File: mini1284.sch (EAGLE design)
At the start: 25 parts, among them U1 ATmega1284P-AU, Y1 16MHz

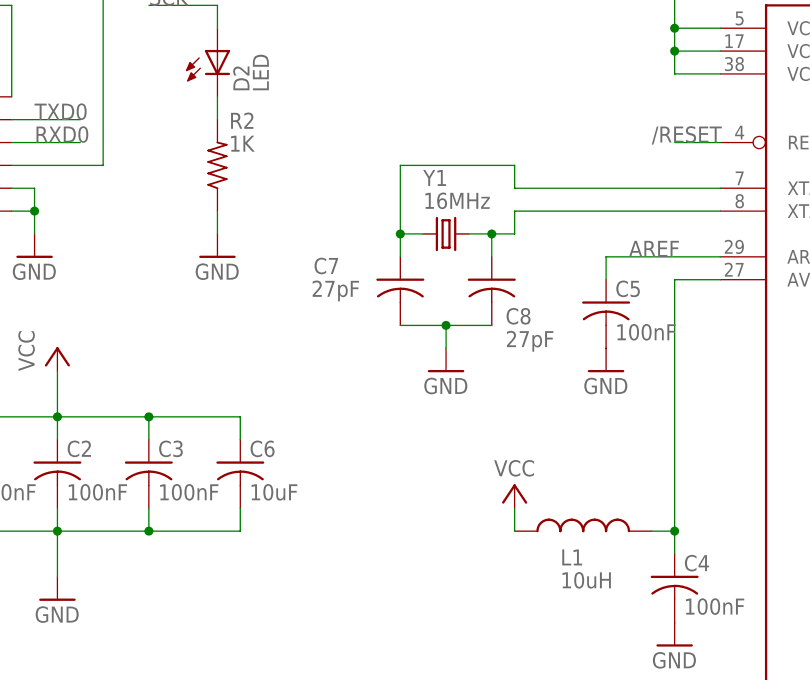
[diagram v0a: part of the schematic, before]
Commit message: Change to Epson crystal.
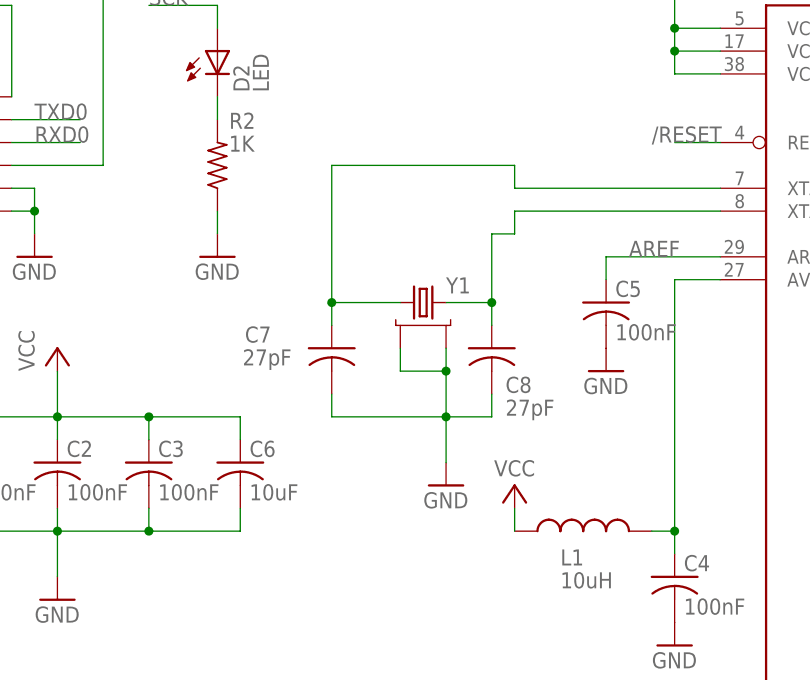
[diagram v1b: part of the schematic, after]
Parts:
- Y1: value 16MHz -> (none); device _jc:CRYSTALABM2 -> _jc:CRYSTAL-2GNDTSX3225
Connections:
- net GND: now also Y1.2, Y1.4
- net N$2: now also Y1.3; no longer Y1.2
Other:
- moved on the sheet: C7, C8
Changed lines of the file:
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@@
 <part name="JP4" library="SparkFun" deviceset="M09" device="" value="M09"/>
 <part name="GND5" library="SparkFun" deviceset="GND" device=""/>
-<part name="Y1" library="_jc" deviceset="CRYSTAL" device="ABM2" value="16MHz"/>
 <part name="P+7" library="supply1" deviceset="VCC" device=""/>
 <part name="GND6" library="SparkFun" deviceset="GND" device=""/>
@@
 <part name="D2" library="_jc" deviceset="LED" device="D0805A" value="LED"/>
 <part name="GND7" library="SparkFun" deviceset="GND" device=""/>
+<part name="Y1" library="_jc" deviceset="CRYSTAL-2GND" device="TSX3225"/>
 </parts>
 <sheets>
@@
 <attribute name="VALUE" x="138.176" y="99.949" size="1.778" layer="96"/>
 </instance>
-<instance part="C7" gate="G$1" x="106.68" y="137.16" smashed="yes">
-<attribute name="NAME" x="97.028" y="137.795" size="1.778" layer="95"/>
-<attribute name="VALUE" x="96.774" y="135.255" size="1.778" layer="96"/>
-</instance>
-<instance part="C8" gate="G$1" x="116.84" y="137.16" smashed="yes">
-<attribute name="NAME" x="118.364" y="132.207" size="1.778" layer="95"/>
-<attribute name="VALUE" x="118.364" y="129.667" size="1.778" layer="96"/>
+<instance part="C7" gate="G$1" x="99.06" y="129.54" smashed="yes">
+<attribute name="NAME" x="89.408" y="130.175" size="1.778" layer="95"/>
+<attribute name="VALUE" x="89.154" y="127.635" size="1.778" layer="96"/>
+</instance>
+<instance part="C8" gate="G$1" x="116.84" y="129.54" smashed="yes">
+<attribute name="NAME" x="118.364" y="124.587" size="1.778" layer="95"/>
+<attribute name="VALUE" x="118.364" y="122.047" size="1.778" layer="96"/>
 </instance>
 <instance part="C6" gate="G$1" x="88.9" y="116.84" smashed="yes">
@@
 <attribute name="VALUE" x="117.094" y="115.316" size="1.778" layer="96"/>
 </instance>
-<instance part="GND3" gate="1" x="111.76" y="127" smashed="yes">
-<attribute name="VALUE" x="109.22" y="124.46" size="1.778" layer="96"/>
+<instance part="GND3" gate="1" x="111.76" y="114.3" smashed="yes">
+<attribute name="VALUE" x="109.22" y="111.76" size="1.778" layer="96"/>
 </instance>
 <instance part="P+6" gate="VCC" x="68.58" y="129.54" smashed="yes">
@@
 <instance part="GND5" gate="1" x="129.54" y="127" smashed="yes">
 <attribute name="VALUE" x="127" y="124.46" size="1.778" layer="96"/>
-</instance>
-<instance part="Y1" gate="G$1" x="111.76" y="142.24" smashed="yes">
-<attribute name="NAME" x="109.22" y="147.574" size="1.778" layer="95"/>
-<attribute name="VALUE" x="109.22" y="145.034" size="1.778" layer="96"/>
 </instance>
 <instance part="P+7" gate="VCC" x="231.14" y="152.4" smashed="yes">
@@
 <attribute name="VALUE" x="83.82" y="137.16" size="1.778" layer="96"/>
 </instance>
+<instance part="Y1" gate="G$1" x="109.22" y="134.62"/>
 </instances>
 <busses>
@@
 <pinref part="C8" gate="G$1" pin="2"/>
 <pinref part="GND3" gate="1" pin="GND"/>
-<wire x1="106.68" y1="132.08" x2="111.76" y2="132.08" width="0.1524" layer="91"/>
-<wire x1="111.76" y1="132.08" x2="111.76" y2="129.54" width="0.1524" layer="91"/>
-<wire x1="116.84" y1="132.08" x2="111.76" y2="132.08" width="0.1524" layer="91"/>
-<junction x="111.76" y="132.08"/>
+<wire x1="99.06" y1="124.46" x2="99.06" y2="121.92" width="0.1524" layer="91"/>
+<wire x1="99.06" y1="121.92" x2="111.76" y2="121.92" width="0.1524" layer="91"/>
+<wire x1="111.76" y1="121.92" x2="111.76" y2="116.84" width="0.1524" layer="91"/>
+<wire x1="116.84" y1="124.46" x2="116.84" y2="121.92" width="0.1524" layer="91"/>
+<wire x1="116.84" y1="121.92" x2="111.76" y2="121.92" width="0.1524" layer="91"/>
+<junction x="111.76" y="121.92"/>
+<pinref part="Y1" gate="G$1" pin="4"/>
+<wire x1="111.76" y1="129.54" x2="111.76" y2="127" width="0.1524" layer="91"/>
+<pinref part="Y1" gate="G$1" pin="2"/>
+<wire x1="111.76" y1="127" x2="111.76" y2="121.92" width="0.1524" layer="91"/>
+<wire x1="106.68" y1="129.54" x2="106.68" y2="127" width="0.1524" layer="91"/>
+<wire x1="106.68" y1="127" x2="111.76" y2="127" width="0.1524" layer="91"/>
+<junction x="111.76" y="127"/>
 </segment>
 <segment>
@@
 <segment>
 <pinref part="U1" gate="G$1" pin="XTAL1"/>
-<wire x1="114.3" y1="142.24" x2="116.84" y2="142.24" width="0.1524" layer="91"/>
 <pinref part="C8" gate="G$1" pin="1"/>
 <wire x1="116.84" y1="142.24" x2="119.38" y2="142.24" width="0.1524" layer="91"/>
 <wire x1="119.38" y1="142.24" x2="119.38" y2="144.78" width="0.1524" layer="91"/>
 <wire x1="119.38" y1="144.78" x2="142.24" y2="144.78" width="0.1524" layer="91"/>
-<wire x1="116.84" y1="139.7" x2="116.84" y2="142.24" width="0.1524" layer="91"/>
-<junction x="116.84" y="142.24"/>
-<pinref part="Y1" gate="G$1" pin="2"/>
+<wire x1="116.84" y1="132.08" x2="116.84" y2="134.62" width="0.1524" layer="91"/>
+<pinref part="Y1" gate="G$1" pin="3"/>
+<wire x1="116.84" y1="134.62" x2="116.84" y2="142.24" width="0.1524" layer="91"/>
+<wire x1="111.76" y1="134.62" x2="116.84" y2="134.62" width="0.1524" layer="91"/>
+<junction x="116.84" y="134.62"/>
 </segment>
 </net>
@@
 <wire x1="119.38" y1="147.32" x2="119.38" y2="149.86" width="0.1524" layer="91"/>
 <pinref part="C7" gate="G$1" pin="1"/>
-<wire x1="119.38" y1="149.86" x2="106.68" y2="149.86" width="0.1524" layer="91"/>
-<wire x1="106.68" y1="149.86" x2="106.68" y2="142.24" width="0.1524" layer="91"/>
-<wire x1="106.68" y1="142.24" x2="106.68" y2="139.7" width="0.1524" layer="91"/>
-<wire x1="106.68" y1="142.24" x2="109.22" y2="142.24" width="0.1524" layer="91"/>
-<junction x="106.68" y="142.24"/>
+<wire x1="119.38" y1="149.86" x2="99.06" y2="149.86" width="0.1524" layer="91"/>
+<wire x1="99.06" y1="149.86" x2="99.06" y2="134.62" width="0.1524" layer="91"/>
+<wire x1="99.06" y1="134.62" x2="99.06" y2="132.08" width="0.1524" layer="91"/>
 <pinref part="Y1" gate="G$1" pin="1"/>
-</segment>
-</net>
+<wire x1="106.68" y1="134.62" x2="99.06" y2="134.62" width="0.1524" layer="91"/>
+<junction x="99.06" y="134.62"/>
+</segment>
+</net>

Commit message: Minor tweaks.
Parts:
- Y1: value (none) -> 16MHz
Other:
- moved on the sheet: C5
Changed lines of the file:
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@@
 <part name="D2" library="_jc" deviceset="LED" device="D0805A" value="LED"/>
 <part name="GND7" library="SparkFun" deviceset="GND" device=""/>
-<part name="Y1" library="_jc" deviceset="CRYSTAL-2GND" device="TSX3225"/>
+<part name="Y1" library="_jc" deviceset="CRYSTAL-2GND" device="TSX3225" value="16MHz"/>
 </parts>
 <sheets>
@@
 <attribute name="VALUE" x="89.916" y="112.649" size="1.778" layer="96"/>
 </instance>
-<instance part="C5" gate="G$1" x="129.54" y="134.62" smashed="yes">
-<attribute name="NAME" x="130.556" y="135.255" size="1.778" layer="95"/>
-<attribute name="VALUE" x="130.556" y="130.429" size="1.778" layer="96"/>
+<instance part="C5" gate="G$1" x="129.54" y="132.08" smashed="yes">
+<attribute name="NAME" x="130.556" y="132.715" size="1.778" layer="95"/>
+<attribute name="VALUE" x="130.556" y="127.889" size="1.778" layer="96"/>
 </instance>
 <instance part="C9" gate="G$1" x="55.88" y="167.64" smashed="yes" rot="R90">
@@
 <attribute name="VALUE" x="117.094" y="115.316" size="1.778" layer="96"/>
 </instance>
-<instance part="GND3" gate="1" x="111.76" y="114.3" smashed="yes">
-<attribute name="VALUE" x="109.22" y="111.76" size="1.778" layer="96"/>
+<instance part="GND3" gate="1" x="111.76" y="116.84" smashed="yes">
+<attribute name="VALUE" x="109.22" y="114.3" size="1.778" layer="96"/>
 </instance>
 <instance part="P+6" gate="VCC" x="68.58" y="129.54" smashed="yes">
@@
 <attribute name="NAME" x="223.52" y="173.99" size="1.778" layer="95" rot="MR0"/>
 </instance>
-<instance part="GND5" gate="1" x="129.54" y="127" smashed="yes">
-<attribute name="VALUE" x="127" y="124.46" size="1.778" layer="96"/>
+<instance part="GND5" gate="1" x="129.54" y="121.92" smashed="yes">
+<attribute name="VALUE" x="127" y="119.38" size="1.778" layer="96"/>
 </instance>
 <instance part="P+7" gate="VCC" x="231.14" y="152.4" smashed="yes">
@@
 <attribute name="VALUE" x="83.82" y="137.16" size="1.778" layer="96"/>
 </instance>
-<instance part="Y1" gate="G$1" x="109.22" y="134.62"/>
+<instance part="Y1" gate="G$1" x="109.22" y="134.62" smashed="yes">
+<attribute name="NAME" x="105.156" y="139.954" size="1.778" layer="95"/>
+<attribute name="VALUE" x="104.902" y="136.906" size="1.778" layer="96"/>
+</instance>
 </instances>
 <busses>
@@
 <wire x1="99.06" y1="124.46" x2="99.06" y2="121.92" width="0.1524" layer="91"/>
 <wire x1="99.06" y1="121.92" x2="111.76" y2="121.92" width="0.1524" layer="91"/>
-<wire x1="111.76" y1="121.92" x2="111.76" y2="116.84" width="0.1524" layer="91"/>
+<wire x1="111.76" y1="121.92" x2="111.76" y2="119.38" width="0.1524" layer="91"/>
 <wire x1="116.84" y1="124.46" x2="116.84" y2="121.92" width="0.1524" layer="91"/>
 <wire x1="116.84" y1="121.92" x2="111.76" y2="121.92" width="0.1524" layer="91"/>
@@
 <pinref part="C5" gate="G$1" pin="2"/>
 <pinref part="GND5" gate="1" pin="GND"/>
+<wire x1="129.54" y1="124.46" x2="129.54" y2="127" width="0.1524" layer="91"/>
 </segment>
 <segment>
@@
 <pinref part="U1" gate="G$1" pin="XTAL1"/>
 <pinref part="C8" gate="G$1" pin="1"/>
-<wire x1="116.84" y1="142.24" x2="119.38" y2="142.24" width="0.1524" layer="91"/>
-<wire x1="119.38" y1="142.24" x2="119.38" y2="144.78" width="0.1524" layer="91"/>
-<wire x1="119.38" y1="144.78" x2="142.24" y2="144.78" width="0.1524" layer="91"/>
+<wire x1="116.84" y1="144.78" x2="142.24" y2="144.78" width="0.1524" layer="91"/>
 <wire x1="116.84" y1="132.08" x2="116.84" y2="134.62" width="0.1524" layer="91"/>
 <pinref part="Y1" gate="G$1" pin="3"/>
-<wire x1="116.84" y1="134.62" x2="116.84" y2="142.24" width="0.1524" layer="91"/>
+<wire x1="116.84" y1="134.62" x2="116.84" y2="144.78" width="0.1524" layer="91"/>
 <wire x1="111.76" y1="134.62" x2="116.84" y2="134.62" width="0.1524" layer="91"/>
 <junction x="116.84" y="134.62"/>
@@
 <segment>
 <pinref part="U1" gate="G$1" pin="XTAL2"/>
-<wire x1="142.24" y1="147.32" x2="119.38" y2="147.32" width="0.1524" layer="91"/>
-<wire x1="119.38" y1="147.32" x2="119.38" y2="149.86" width="0.1524" layer="91"/>
+<wire x1="142.24" y1="147.32" x2="99.06" y2="147.32" width="0.1524" layer="91"/>
 <pinref part="C7" gate="G$1" pin="1"/>
-<wire x1="119.38" y1="149.86" x2="99.06" y2="149.86" width="0.1524" layer="91"/>
-<wire x1="99.06" y1="149.86" x2="99.06" y2="134.62" width="0.1524" layer="91"/>
+<wire x1="99.06" y1="147.32" x2="99.06" y2="134.62" width="0.1524" layer="91"/>
 <wire x1="99.06" y1="134.62" x2="99.06" y2="132.08" width="0.1524" layer="91"/>
 <pinref part="Y1" gate="G$1" pin="1"/>
@@
 <pinref part="C5" gate="G$1" pin="1"/>
 <pinref part="U1" gate="G$1" pin="AREF"/>
-<wire x1="129.54" y1="137.16" x2="129.54" y2="139.7" width="0.1524" layer="91"/>
+<wire x1="129.54" y1="134.62" x2="129.54" y2="139.7" width="0.1524" layer="91"/>
 <wire x1="129.54" y1="139.7" x2="142.24" y2="139.7" width="0.1524" layer="91"/>
 <label x="132.08" y="139.7" size="1.778" layer="95"/>
